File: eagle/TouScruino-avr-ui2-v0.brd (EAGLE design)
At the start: 63.5 x 72.4 mm, 60 parts, among them J1 AVR_ISP, Q1 8MHz, Q2 MMBT2222A, Q3 8MHz, U1 ATMEGA1284P, U2 AR1021, U3 MIC5209-3.3YS, U4 MCP73831, X2 USB

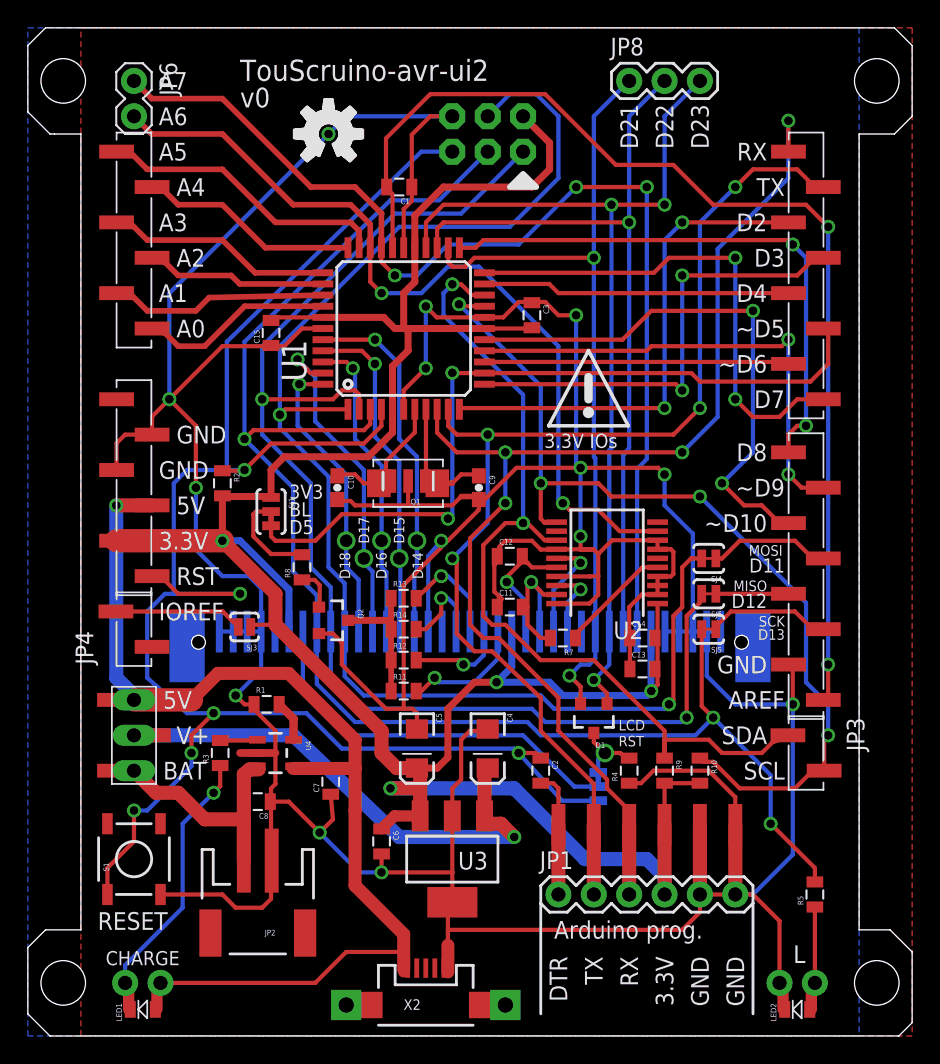
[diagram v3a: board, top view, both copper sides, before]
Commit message: 
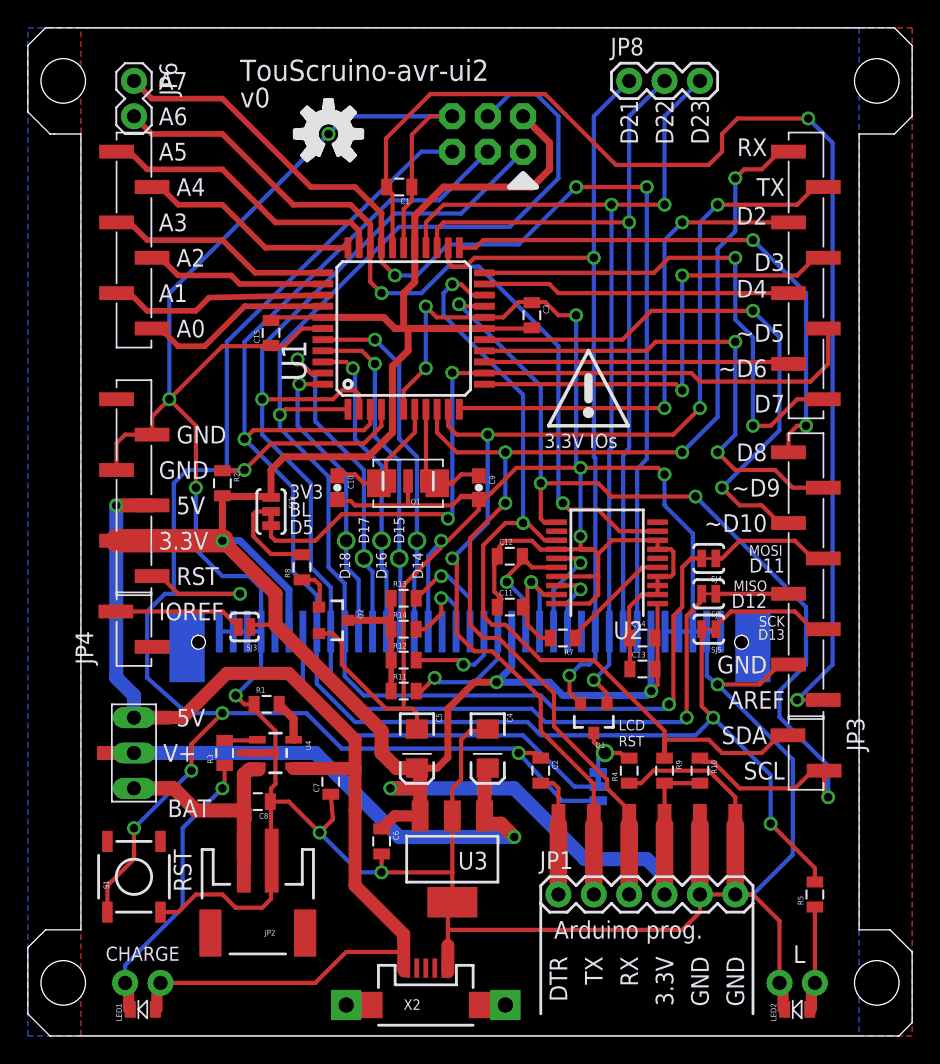
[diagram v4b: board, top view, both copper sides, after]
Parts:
- moved JP5 1.27 mm to (7.62, 17.8)
- moved S1 1.27 mm to (7.62, 11.4)
- moved R3 0.32 mm to (14.1, 20.3)
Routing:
- net AREF: track 80.3 -> 90.5 mm
- net D19/SCL: track 68.0 -> 73.2 mm
- net D0/RX: track 87.3 -> 83.9 mm
- net VUSB: track 85.3 -> 87.1 mm
- net D10/PWM4: track 39.3 -> 41.1 mm
- net D8: track 40.5 -> 39.0 mm
- net GND: track 402.8 -> 404.2 mm
- net D1/TX: track 83.7 -> 82.6 mm
- net RES: track 133.0 -> 133.9 mm
- net D7: track 36.0 -> 36.9 mm
- net D9/PWM3: track 34.8 -> 35.4 mm
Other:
- board text removed: "RESET"
